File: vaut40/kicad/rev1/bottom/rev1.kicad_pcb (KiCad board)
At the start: 2 copper layers, 228.3 x 111.8 mm, 0 parts

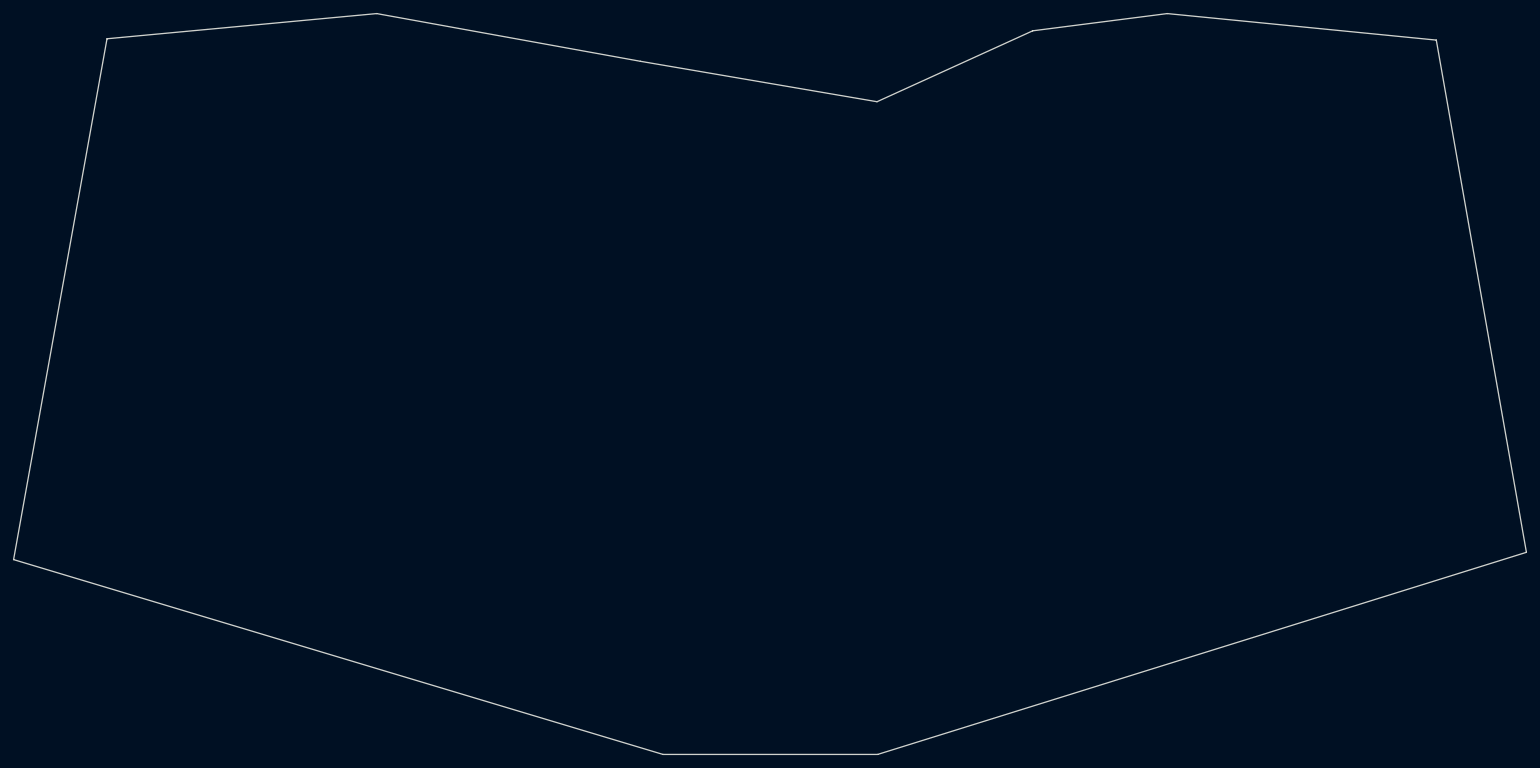
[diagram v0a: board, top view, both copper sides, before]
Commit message: add hole of bottom
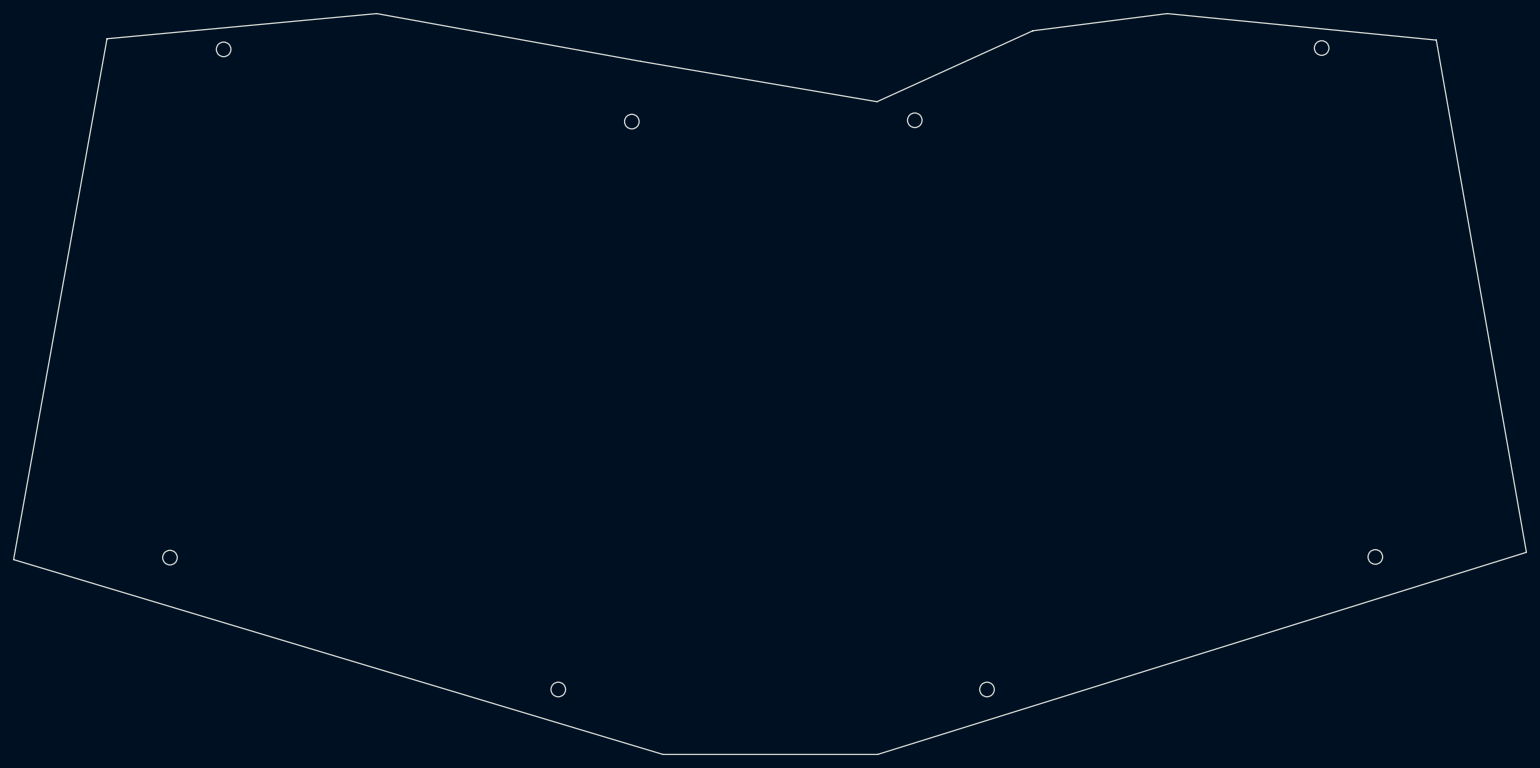
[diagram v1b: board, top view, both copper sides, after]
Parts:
- added Ref**: Val**, kbd_Hole:m2_Screw_Hole, F.Cu at (186.6, 143.8)
- added Ref**: Val**, kbd_Hole:m2_Screw_Hole, F.Cu at (175.7, 57.9)
- added Ref**: Val**, kbd_Hole:m2_Screw_Hole, F.Cu at (245.2, 123.8)
- added Ref**: Val**, kbd_Hole:m2_Screw_Hole, F.Cu at (63.3, 123.9)
- added Ref**: Val**, kbd_Hole:m2_Screw_Hole, F.Cu at (121.9, 143.8)
- added Ref**: Val**, kbd_Hole:m2_Screw_Hole, F.Cu at (237.1, 47.0)
- added Ref**: Val**, kbd_Hole:m2_Screw_Hole, F.Cu at (133.0, 58.1)
- added Ref**: Val**, kbd_Hole:m2_Screw_Hole, F.Cu at (71.4, 47.2)
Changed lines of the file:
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@@
   )
   (net 0 "")
+  (footprint "kbd_Hole:m2_Screw_Hole" (layer "F.Cu")
+    (at 186.6 143.8)
+    (descr "Mounting Hole 2.2mm, no annular, M2")
+    (tags "mounting hole 2.2mm no annular m2")
+    (attr exclude_from_pos_files exclude_from_bom)
+    (fp_text reference "Ref**" (at 0 -3.2) (layer "F.Fab")
+        (effects (font (size 1 1) (thickness 0.15)))
+    )
+    (fp_text value "Val**" (at 0 3.2) (layer "F.Fab")
+        (effects (font (size 1 1) (thickness 0.15)))
+    )
+    (fp_text user "${REFERENCE}" (at 0.3 0) (layer "F.Fab")
+        (effects (font (size 1 1) (thickness 0.15)))
+    )
+    (fp_circle (center 0 0) (end 2.2 0)
+      (stroke (width 0.15) (type solid)) (fill none) (layer "Cmts.User"))
+    (fp_circle (center 0 0) (end 2.45 0)
+      (stroke (width 0.05) (type solid)) (fill none) (layer "F.CrtYd"))
+    (pad "" np_thru_hole circle (at 0 0) (size 2.2 2.2) (drill 2.2) (layers "F&B.Cu" "*.Mask"))
+  )
+  (footprint "kbd_Hole:m2_Screw_Hole" (layer "F.Cu")
+    (at 175.7 57.9)
+    (descr "Mounting Hole 2.2mm, no annular, M2")
+    (tags "mounting hole 2.2mm no annular m2")
+    (attr exclude_from_pos_files exclude_from_bom)
+    (fp_text reference "Ref**" (at 0 -3.2) (layer "F.Fab")
+        (effects (font (size 1 1) (thickness 0.15)))
+    )
+    (fp_text value "Val**" (at 0 3.2) (layer "F.Fab")
+        (effects (font (size 1 1) (thickness 0.15)))
+    )
+    (fp_text user "${REFERENCE}" (at 0.3 0) (layer "F.Fab")
+        (effects (font (size 1 1) (thickness 0.15)))
+    )
+    (fp_circle (center 0 0) (end 2.2 0)
+      (stroke (width 0.15) (type solid)) (fill none) (layer "Cmts.User"))
+    (fp_circle (center 0 0) (end 2.45 0)
+      (stroke (width 0.05) (type solid)) (fill none) (layer "F.CrtYd"))
+    (pad "" np_thru_hole circle (at 0 0) (size 2.2 2.2) (drill 2.2) (layers "F&B.Cu" "*.Mask"))
+  )
+  (footprint "kbd_Hole:m2_Screw_Hole" (layer "F.Cu")
+    (at 245.2 123.8)
+    (descr "Mounting Hole 2.2mm, no annular, M2")
+    (tags "mounting hole 2.2mm no annular m2")
+    (attr exclude_from_pos_files exclude_from_bom)
+    (fp_text reference "Ref**" (at 0 -3.2) (layer "F.Fab")
+        (effects (font (size 1 1) (thickness 0.15)))
+    )
+    (fp_text value "Val**" (at 0 3.2) (layer "F.Fab")
+        (effects (font (size 1 1) (thickness 0.15)))
+    )
+    (fp_text user "${REFERENCE}" (at 0.3 0) (layer "F.Fab")
+        (effects (font (size 1 1) (thickness 0.15)))
+    )
+    (fp_circle (center 0 0) (end 2.2 0)
+      (stroke (width 0.15) (type solid)) (fill none) (layer "Cmts.User"))
+    (fp_circle (center 0 0) (end 2.45 0)
+      (stroke (width 0.05) (type solid)) (fill none) (layer "F.CrtYd"))
+    (pad "" np_thru_hole circle (at 0 0) (size 2.2 2.2) (drill 2.2) (layers "F&B.Cu" "*.Mask"))
+  )
+  (footprint "kbd_Hole:m2_Screw_Hole" (layer "F.Cu")
+    (at 63.3 123.9)
+    (descr "Mounting Hole 2.2mm, no annular, M2")
+    (tags "mounting hole 2.2mm no annular m2")
+    (attr exclude_from_pos_files exclude_from_bom)
+    (fp_text reference "Ref**" (at 0 -3.2) (layer "F.Fab")
+        (effects (font (size 1 1) (thickness 0.15)))
+    )
+    (fp_text value "Val**" (at 0 3.2) (layer "F.Fab")
+        (effects (font (size 1 1) (thickness 0.15)))
+    )
+    (fp_text user "${REFERENCE}" (at 0.3 0) (layer "F.Fab")
+        (effects (font (size 1 1) (thickness 0.15)))
+    )
+    (fp_circle (center 0 0) (end 2.2 0)
+      (stroke (width 0.15) (type solid)) (fill none) (layer "Cmts.User"))
+    (fp_circle (center 0 0) (end 2.45 0)
+      (stroke (width 0.05) (type solid)) (fill none) (layer "F.CrtYd"))
+    (pad "" np_thru_hole circle (at 0 0) (size 2.2 2.2) (drill 2.2) (layers "F&B.Cu" "*.Mask"))
+  )
+  (footprint "kbd_Hole:m2_Screw_Hole" (layer "F.Cu")
+    (at 121.9 143.8)
+    (descr "Mounting Hole 2.2mm, no annular, M2")
+    (tags "mounting hole 2.2mm no annular m2")
+    (attr exclude_from_pos_files exclude_from_bom)
+    (fp_text reference "Ref**" (at 0 -3.2) (layer "F.Fab")
+        (effects (font (size 1 1) (thickness 0.15)))
+    )
+    (fp_text value "Val**" (at 0 3.2) (layer "F.Fab")
+        (effects (font (size 1 1) (thickness 0.15)))
+    )
+    (fp_text user "${REFERENCE}" (at 0.3 0) (layer "F.Fab")
+        (effects (font (size 1 1) (thickness 0.15)))
+    )
+    (fp_circle (center 0 0) (end 2.2 0)
+      (stroke (width 0.15) (type solid)) (fill none) (layer "Cmts.User"))
+    (fp_circle (center 0 0) (end 2.45 0)
+      (stroke (width 0.05) (type solid)) (fill none) (layer "F.CrtYd"))
+    (pad "" np_thru_hole circle (at 0 0) (size 2.2 2.2) (drill 2.2) (layers "F&B.Cu" "*.Mask"))
+  )
+  (footprint "kbd_Hole:m2_Screw_Hole" (layer "F.Cu")
+    (at 237.1 47)
+    (descr "Mounting Hole 2.2mm, no annular, M2")
+    (tags "mounting hole 2.2mm no annular m2")
+    (attr exclude_from_pos_files exclude_from_bom)
+    (fp_text reference "Ref**" (at 0 -3.2) (layer "F.Fab")
+        (effects (font (size 1 1) (thickness 0.15)))
+    )
+    (fp_text value "Val**" (at 0 3.2) (layer "F.Fab")
+        (effects (font (size 1 1) (thickness 0.15)))
+    )
+    (fp_text user "${REFERENCE}" (at 0.3 0) (layer "F.Fab")
+        (effects (font (size 1 1) (thickness 0.15)))
+    )
+    (fp_circle (center 0 0) (end 2.2 0)
+      (stroke (width 0.15) (type solid)) (fill none) (layer "Cmts.User"))
+    (fp_circle (center 0 0) (end 2.45 0)
+      (stroke (width 0.05) (type solid)) (fill none) (layer "F.CrtYd"))
+    (pad "" np_thru_hole circle (at 0 0) (size 2.2 2.2) (drill 2.2) (layers "F&B.Cu" "*.Mask"))
+  )
+  (footprint "kbd_Hole:m2_Screw_Hole" (layer "F.Cu")
+    (at 133 58.1)
+    (descr "Mounting Hole 2.2mm, no annular, M2")
+    (tags "mounting hole 2.2mm no annular m2")
+    (attr exclude_from_pos_files exclude_from_bom)
+    (fp_text reference "Ref**" (at 0 -3.2) (layer "F.Fab")
+        (effects (font (size 1 1) (thickness 0.15)))
+    )
+    (fp_text value "Val**" (at 0 3.2) (layer "F.Fab")
+        (effects (font (size 1 1) (thickness 0.15)))
+    )
+    (fp_text user "${REFERENCE}" (at 0.3 0) (layer "F.Fab")
+        (effects (font (size 1 1) (thickness 0.15)))
+    )
+    (fp_circle (center 0 0) (end 2.2 0)
+      (stroke (width 0.15) (type solid)) (fill none) (layer "Cmts.User"))
+    (fp_circle (center 0 0) (end 2.45 0)
+      (stroke (width 0.05) (type solid)) (fill none) (layer "F.CrtYd"))
+    (pad "" np_thru_hole circle (at 0 0) (size 2.2 2.2) (drill 2.2) (layers "F&B.Cu" "*.Mask"))
+  )
+  (footprint "kbd_Hole:m2_Screw_Hole" (layer "F.Cu")
+    (at 71.4 47.2)
+    (descr "Mounting Hole 2.2mm, no annular, M2")
+    (tags "mounting hole 2.2mm no annular m2")
+    (attr exclude_from_pos_files exclude_from_bom)
+    (fp_text reference "Ref**" (at 0 -3.2) (layer "F.Fab")
+        (effects (font (size 1 1) (thickness 0.15)))
+    )
+    (fp_text value "Val**" (at 0 3.2) (layer "F.Fab")
+        (effects (font (size 1 1) (thickness 0.15)))
+    )
+    (fp_text user "${REFERENCE}" (at 0.3 0) (layer "F.Fab")
+        (effects (font (size 1 1) (thickness 0.15)))
+    )
+    (fp_circle (center 0 0) (end 2.2 0)
+      (stroke (width 0.15) (type solid)) (fill none) (layer "Cmts.User"))
+    (fp_circle (center 0 0) (end 2.45 0)
+      (stroke (width 0.05) (type solid)) (fill none) (layer "F.CrtYd"))
+    (pad "" np_thru_hole circle (at 0 0) (size 2.2 2.2) (drill 2.2) (layers "*.Cu" "*.Mask"))
+  )
   (gr_line (start 193.5 44.4) (end 213.8 41.8)
     (stroke (width 0.1) (type default)) (layer "Edge.Cuts"))
